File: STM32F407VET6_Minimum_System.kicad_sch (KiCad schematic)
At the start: 20 parts, among them SW1 SW_DIP_x01, U1 STM32F407VET, Y1 8MHz

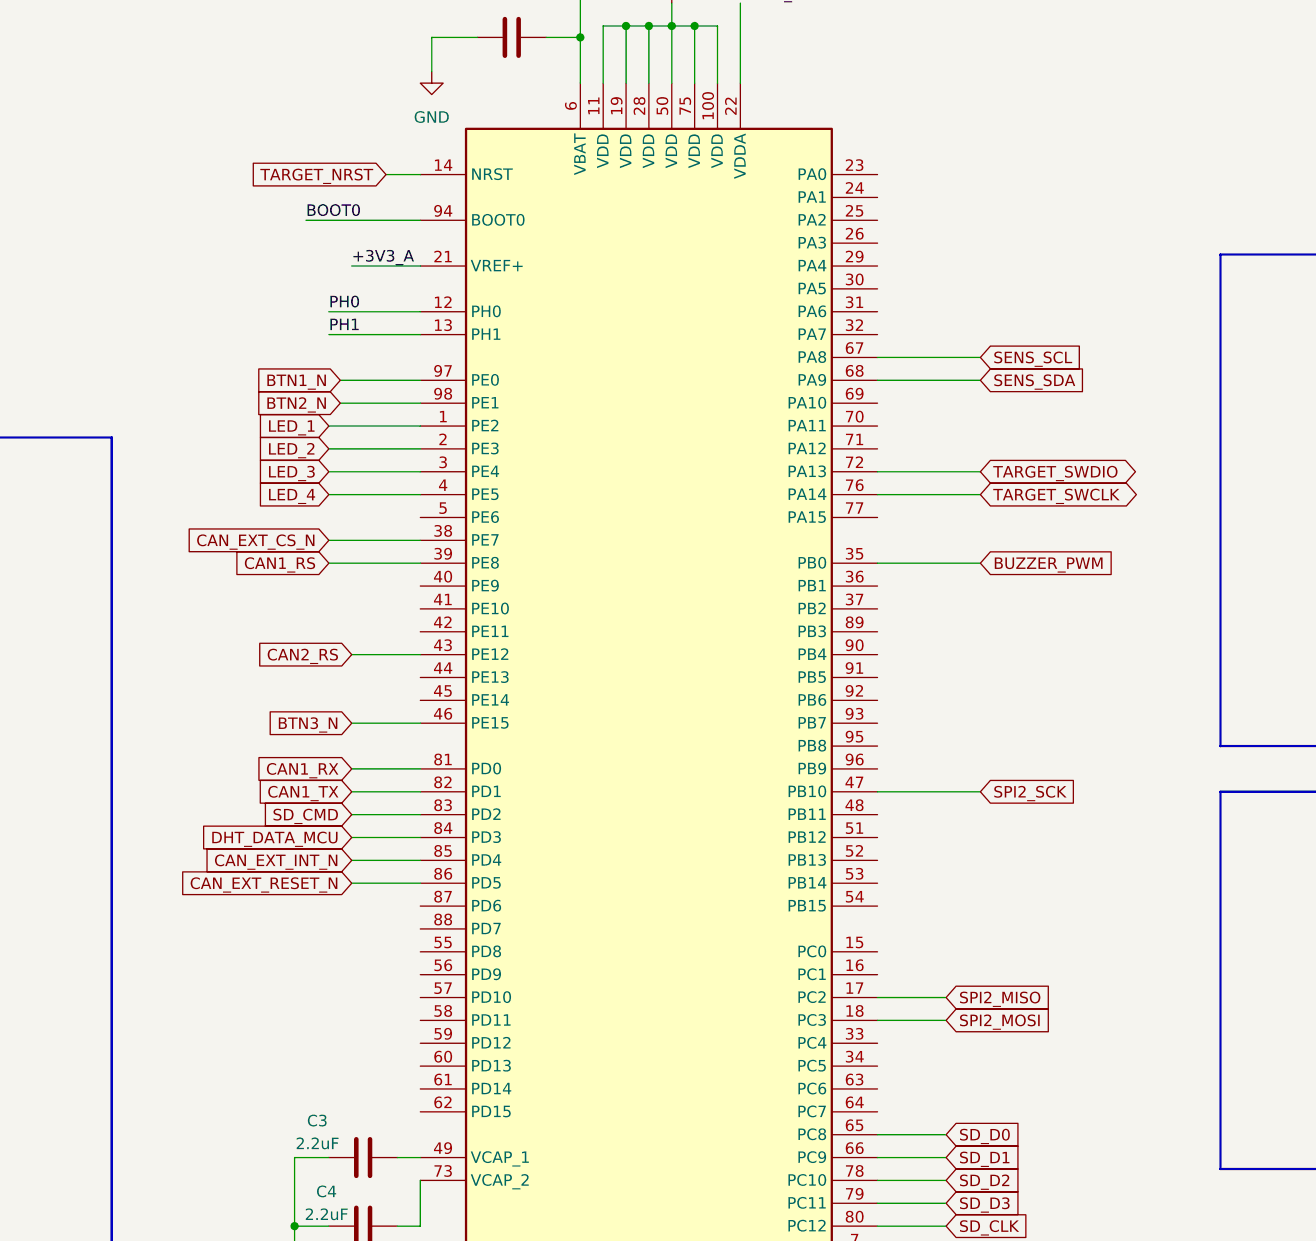
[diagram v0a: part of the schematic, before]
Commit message: feat: implement analog and timer block
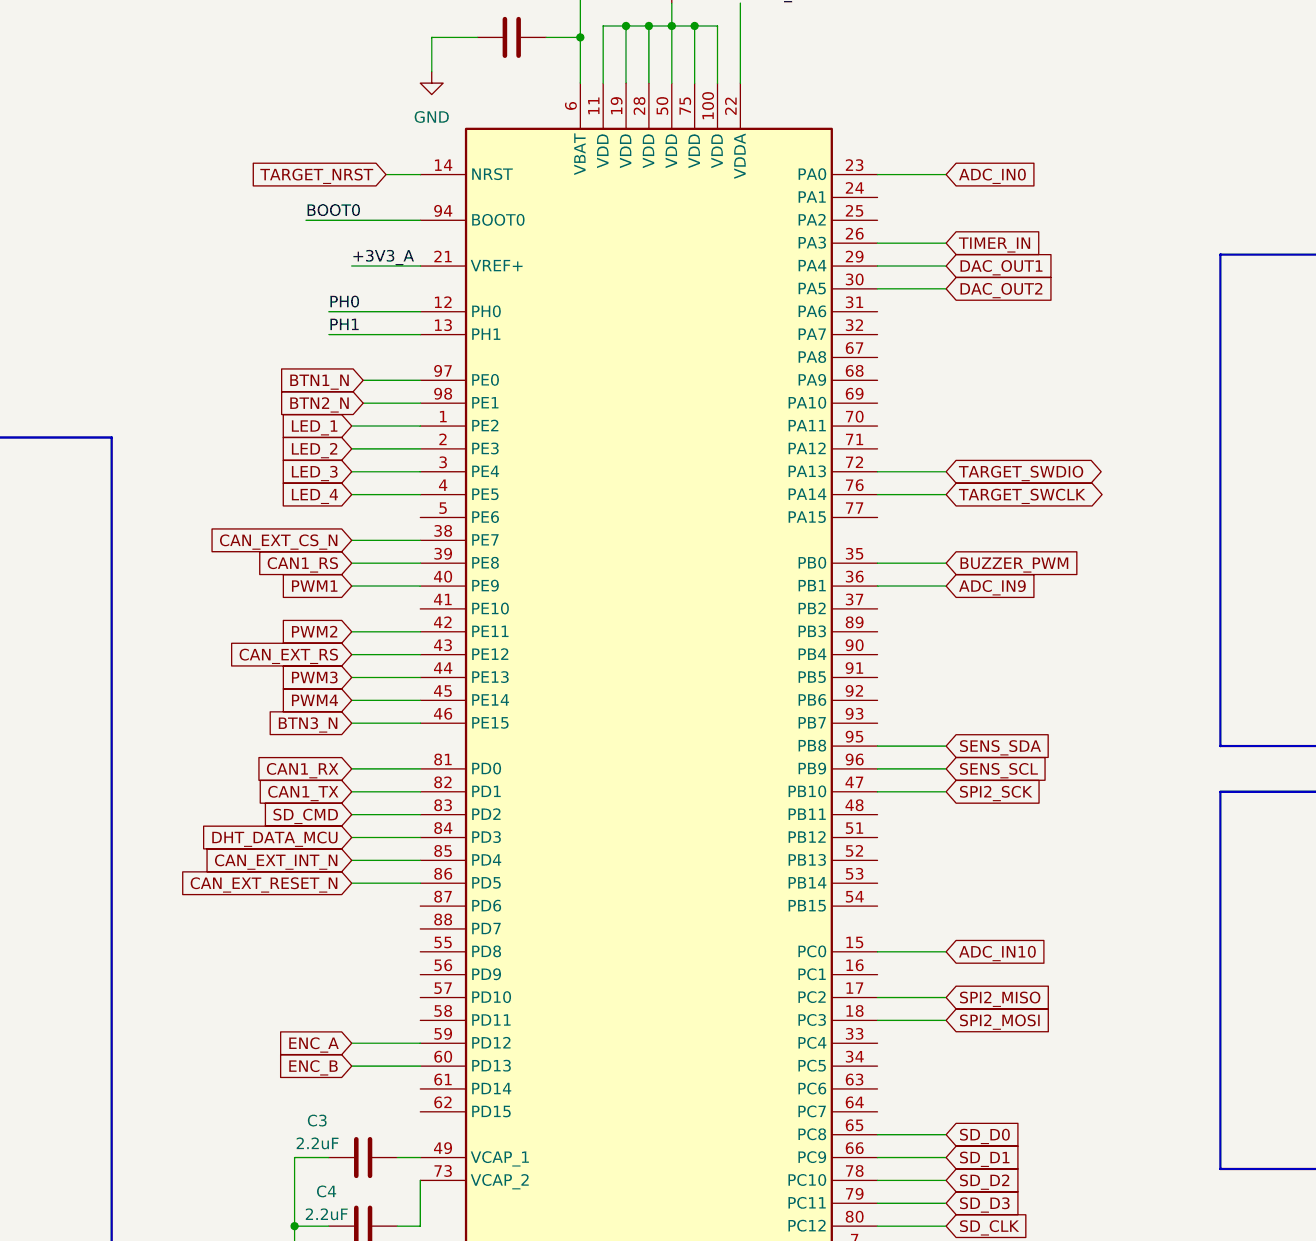
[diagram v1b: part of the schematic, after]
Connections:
- net SENS_SCL: now also U1.96 (PB9); no longer U1.67 (PA8)
- net SENS_SDA: now also U1.95 (PB8); no longer U1.68 (PA9)
- net ADC_IN10: now reaches U1.15 (PC0)
- net ADC_IN0: now reaches U1.23 (PA0)
- net TIMER_IN: now reaches U1.26 (PA3)
- net DAC_OUT1: now reaches U1.29 (PA4)
- net DAC_OUT2: now reaches U1.30 (PA5)
- net ADC_IN9: now reaches U1.36 (PB1)
- net PWM1: now reaches U1.40 (PE9)
- net PWM2: now reaches U1.42 (PE11)
- net PWM3: now reaches U1.44 (PE13)
- net PWM4: now reaches U1.45 (PE14)
- net ENC_A: now reaches U1.59 (PD12)
- net ENC_B: now reaches U1.60 (PD13)
- net CAN2_RS renamed CAN_EXT_RS

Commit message: feat: implement precision adc
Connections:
- net SENS_SCL: now also U1.95 (PB8); no longer U1.96 (PB9)
- net SENS_SDA: now also U1.96 (PB9); no longer U1.95 (PB8)
- net ADC_EXT_DRDY_N: now reaches U1.87 (PD6)
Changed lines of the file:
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@@
+	(wire
+		(pts
+			(xy 172.72 132.08) (xy 180.34 132.08)
+		)
+		(stroke
+			(width 0)
+			(type default)
+		)
+	)
 	(wire
 		(pts
@@
 				)
 				(justify left)
+			)
+		)
+	)
+	(global_label "ADC_EXT_DRDY_N"
+		(shape input)
+		(at 172.72 132.08 180)
+		(fields_autoplaced yes)
+		(effects
+			(font
+				(size 1.27 1.27)
+			)
+			(justify right)
+		)
+		(property "Intersheetrefs" "${INTERSHEET_REFS}"
+			(at 153.6482 132.08 0)
+			(hide yes)
+			(show_name no)
+			(do_not_autoplace no)
+			(effects
+				(font
+					(size 1.27 1.27)
+				)
+				(justify right)
 			)
 		)
@@
 	(global_label "SENS_SCL"
 		(shape input)
-		(at 238.76 116.84 0)
+		(at 238.76 114.3 0)
 		(fields_autoplaced yes)
 		(effects
@@
 		)
 		(property "Intersheetrefs" "${INTERSHEET_REFS}"
-			(at 251.1189 116.84 0)
+			(at 251.1189 114.3 0)
 			(hide yes)
 			(show_name no)
@@
 	(global_label "SENS_SDA"
 		(shape input)
-		(at 238.76 114.3 0)
+		(at 238.76 116.84 0)
 		(fields_autoplaced yes)
 		(effects
@@
 		)
 		(property "Intersheetrefs" "${INTERSHEET_REFS}"
-			(at 251.1794 114.3 0)
-			(hide yes)
-			(show_name no)
+			(at 251.1794 116.84 0)
+			(hide yes)
+			(show_name no)

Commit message: feat(ethernet): add LAN8720A PHY and RJ45 MagJack schematic
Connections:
- net ETH_MDC: now reaches U1.16 (PC1)
- net ETH_REF_CLK: now reaches U1.24 (PA1)
- net ETH_MDIO: now reaches U1.25 (PA2)
- net ETH_CRS_DV: now reaches U1.32 (PA7)
- net ETH_RXD0: now reaches U1.33 (PC4)
- net ETH_RXD1: now reaches U1.34 (PC5)
- net ADC_EXT_CS_N: now reaches U1.41 (PE10)
- net ETH_TX_EN: now reaches U1.48 (PB11)
- net ETH_TXD0: now reaches U1.51 (PB12)
- net ETH_TXD1: now reaches U1.52 (PB13)
- net ETH_RESET_N: now reaches U1.57 (PD10)
